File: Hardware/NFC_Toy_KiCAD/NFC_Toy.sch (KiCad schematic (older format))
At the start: 29 parts

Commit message: Ready to start layout
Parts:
- added D1, D2: LED, symbol LED
- added J10, J11, J12, J14, J3, J4, J5, J6, J7, J8, J9: TP, symbol TEST_1P
- added R1, R2: 121, symbol R
- R7: renamed from R?; value R -> 10k
- gave numbers to parts that had none: 28
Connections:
- net labels added: DotStar_Clk_3V, DotStar_Data_3V
- wire segments 132 -> 152
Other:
- note added: "Accelerometer"
- note added: "J-Link"
- note added: "Power Supply"
- note added: "uC"
- moved on the sheet: C1, C10, C11, C12, C13, C2, C3, C4, C5, C6, C7, C8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

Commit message: Layout started
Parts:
- removed J10, J11, J12, J14, J3, J4, J5, J6, J7, J8, J9: TP, symbol TEST_1P
- added TP1, TP10, TP11, TP2, TP3, TP4, TP5, TP6, TP7, TP8, TP9: TEST, NFC_Toy_Lib:Test_Point, symbol TEST
- C1, C12, C13, C2, C3, C4, C5, C6: footprint (none) -> Capacitors_SMD:C_0402
- C10, C11, C7, C8: footprint (none) -> Capacitors_SMD:C_0603_HandSoldering
- C9: footprint (none) -> Capacitors_SMD:C_1206_HandSoldering
- D1, D2: footprint (none) -> LEDs:LED_0603_HandSoldering
- J1, J2: footprint (none) -> NFC_Toy_Lib:Pad_SMD_Small
- J3: renamed from J13; footprint MODULE -> Socket_Strips:Socket_Strip_Straight_2x05_Pitch2.54mm_SMD
- L1: footprint (none) -> Inductors_SMD:L_12x12mm_h4.5mm
- R1, R10, R2, R3, R4, R5, R6, R7, R8, R9: footprint (none) -> Resistors_SMD:R_0603_HandSoldering
- U1: footprint SOP65P640X120-17N -> NFC_Toy_Lib:SOP65P640X120-17N
- U19: footprint SOT95P280X130-5N -> TO_SOT_Packages_SMD:SOT-23-5
- U2: footprint QFP50P900X900X160-48N -> NFC_Toy_Lib:QFP50P900X900X160-48N
- U3: footprint (none) -> NFC_Toy_Lib:LGA16R50P5X3_300X300X100N
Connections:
- wire segments 152 -> 151
- no-connect marks 9 -> 22
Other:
- moved on the sheet: R9

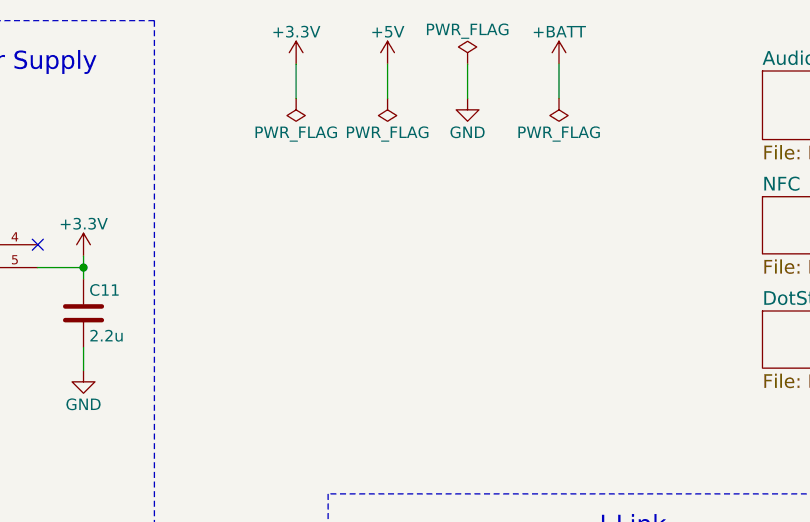
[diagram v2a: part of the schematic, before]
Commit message: Component placement complete.
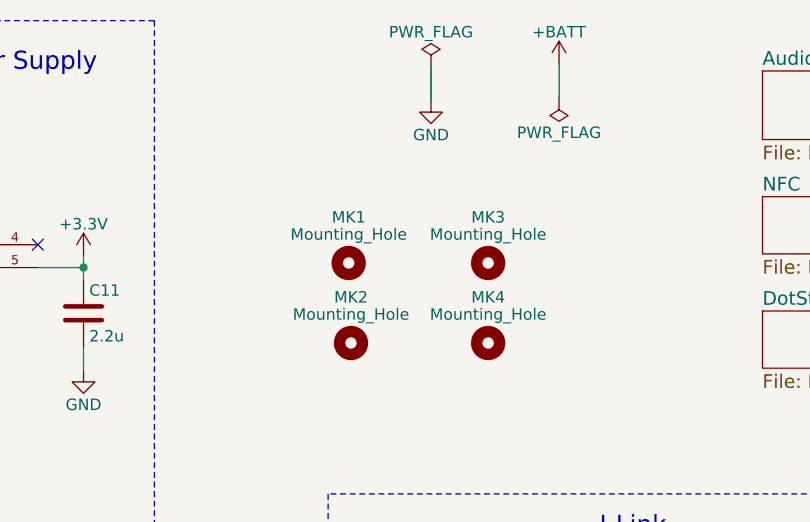
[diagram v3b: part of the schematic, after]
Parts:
- added MK1, MK2, MK3, MK4: Mounting_Hole, Mounting_Holes:MountingHole_2.5mm, symbol Mounting_Hole

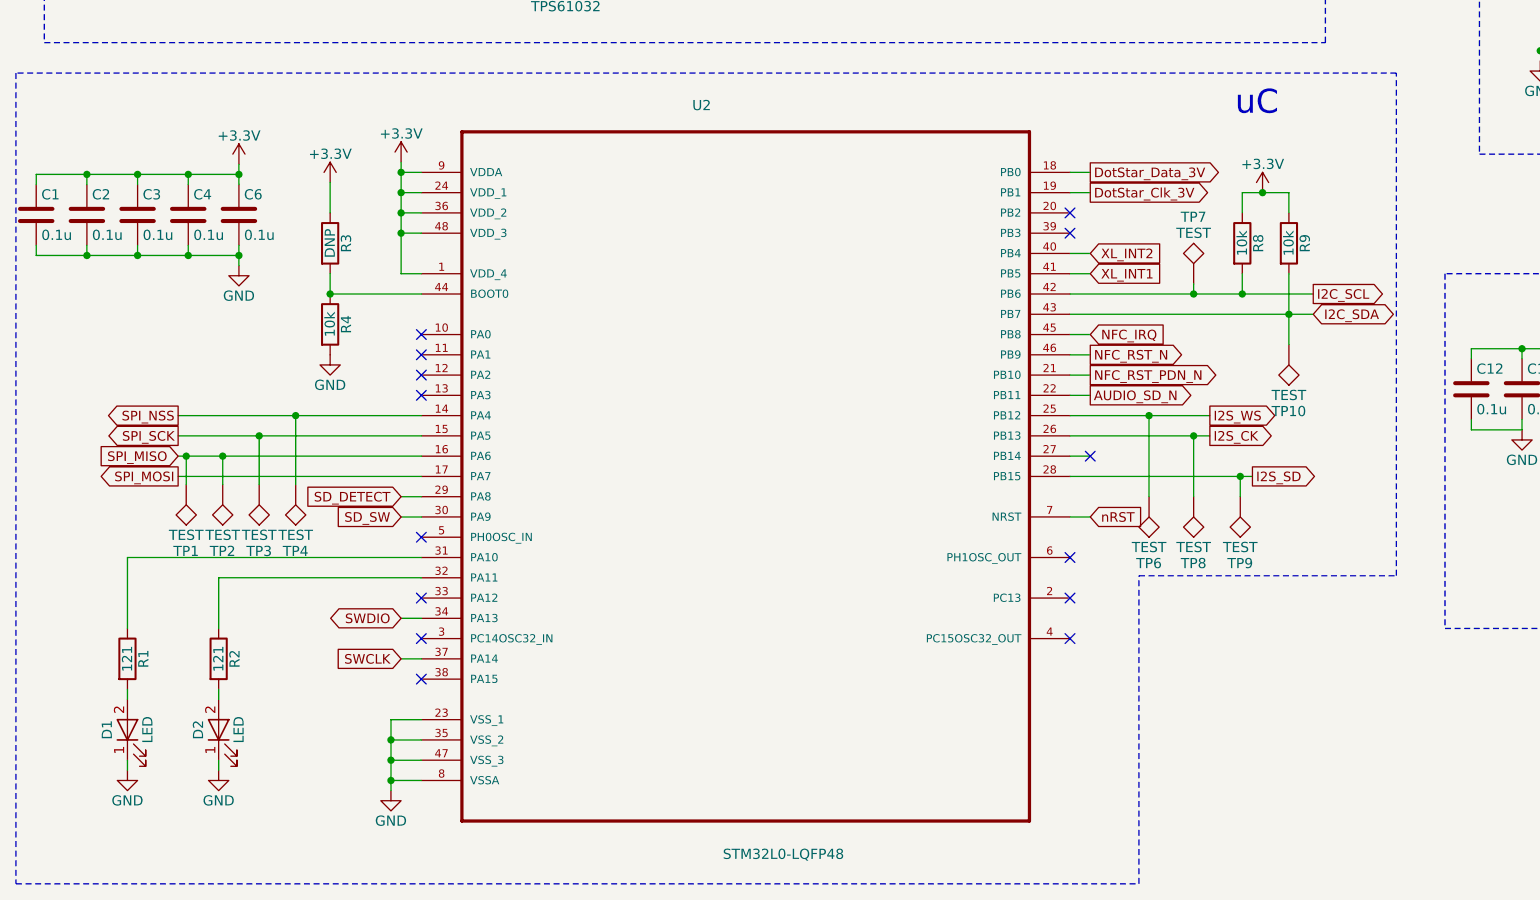
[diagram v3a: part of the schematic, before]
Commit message: Layout 75% complete
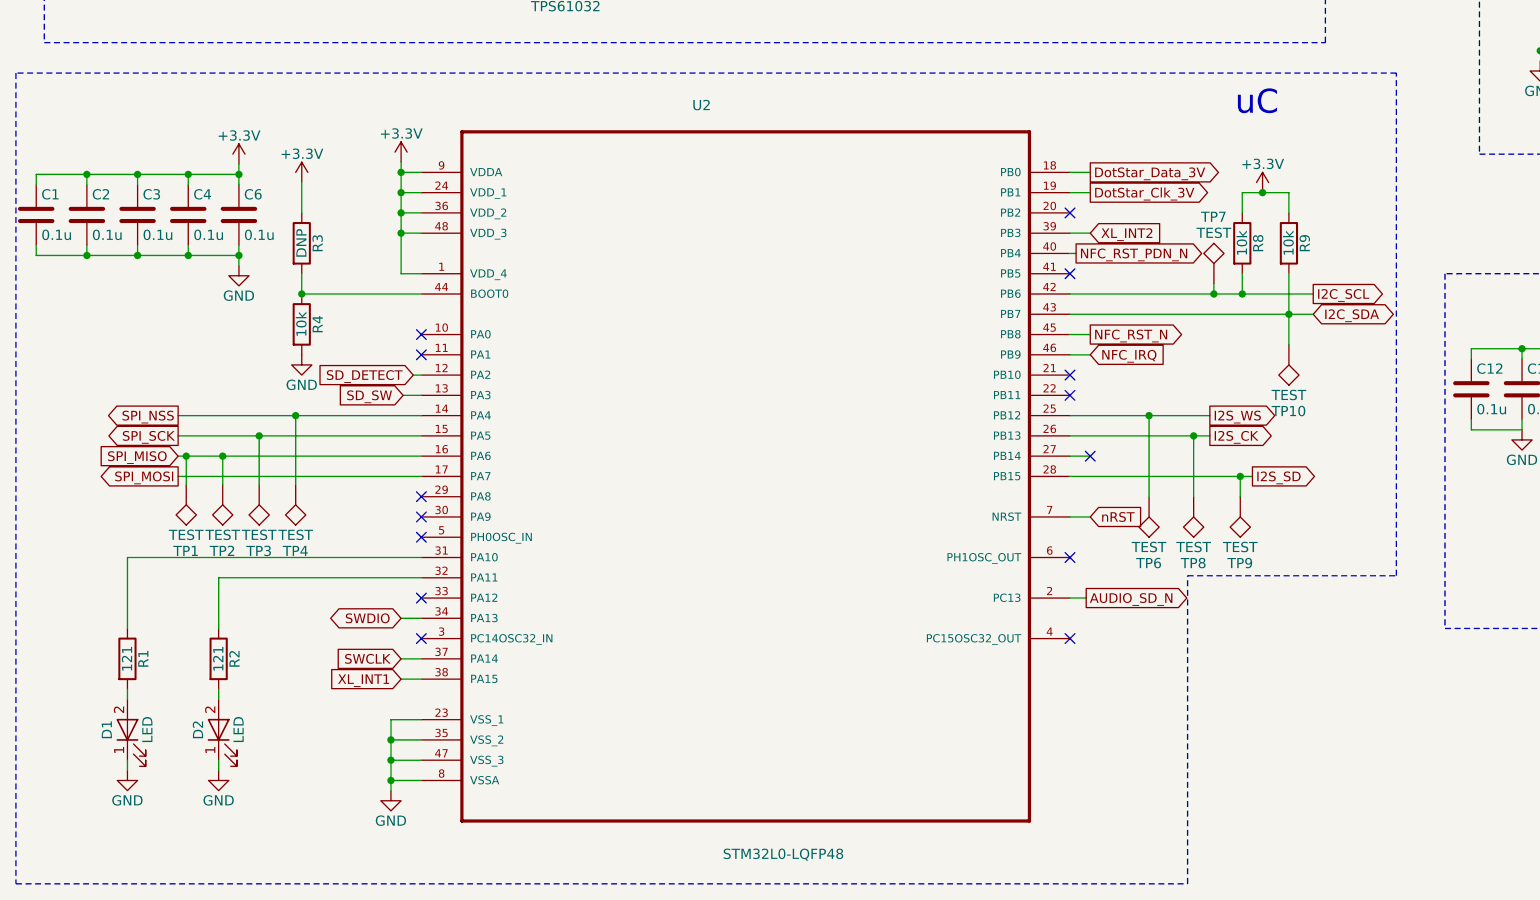
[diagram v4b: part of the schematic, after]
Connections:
- net AUDIO_SD_N: now also U2.2 (PC13); no longer U2.22 (PB11)
- net NFC_IRQ: now also U2.46 (PB9); no longer U2.45 (PB8)
- net NFC_RST_N: now also U2.45 (PB8); no longer U2.46 (PB9)
- net NFC_RST_PDN_N: now also U2.40 (PB4); no longer U2.21 (PB10)
- net SD_DETECT: now also U2.12 (PA2); no longer U2.29 (PA8)
- net SD_SW: now also U2.13 (PA3); no longer U2.30 (PA9)
- net XL_INT1: now also U2.38 (PA15); no longer U2.41 (PB5)
- net XL_INT2: now also U2.39 (PB3); no longer U2.40 (PB4)
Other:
- moved on the sheet: R3, R4, TP7
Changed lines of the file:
@@
 L R R4
 U 1 1 5AC7A59A
-P 2210 4880
-F 0 "R4" V 2290 4880 50  0000 C CNN
-F 1 "10k" V 2210 4880 50  0000 C CNN
-F 2 "Resistors_SMD:R_0603_HandSoldering" V 2140 4880 50  0001 C CNN
-F 3 "" H 2210 4880 50  0001 C CNN
-	1    2210 4880
+P 2070 4880
+F 0 "R4" V 2150 4880 50  0000 C CNN
+F 1 "10k" V 2070 4880 50  0000 C CNN
+F 2 "Resistors_SMD:R_0603_HandSoldering" V 2000 4880 50  0001 C CNN
+F 3 "" H 2070 4880 50  0001 C CNN
+	1    2070 4880
 	1    0    0    -1
 $EndComp
@@
 L R R3
 U 1 1 5ACB59B1
-P 2210 4480
-F 0 "R3" V 2290 4480 50  0000 C CNN
-F 1 "DNP" V 2210 4480 50  0000 C CNN
-F 2 "Resistors_SMD:R_0603_HandSoldering" V 2140 4480 50  0001 C CNN
-F 3 "" H 2210 4480 50  0001 C CNN
-	1    2210 4480
+P 2070 4480
+F 0 "R3" V 2150 4480 50  0000 C CNN
+F 1 "DNP" V 2070 4480 50  0000 C CNN
+F 2 "Resistors_SMD:R_0603_HandSoldering" V 2000 4480 50  0001 C CNN
+F 3 "" H 2070 4480 50  0001 C CNN
+	1    2070 4480
 	1    0    0    -1
 $EndComp
@@
 L +3.3V #PWR021
 U 1 1 5ACD275B
-P 2210 4180
-F 0 "#PWR021" H 2210 4030 50  0001 C CNN
-F 1 "+3.3V" H 2210 4320 50  0000 C CNN
-F 2 "" H 2210 4180 50  0001 C CNN
-F 3 "" H 2210 4180 50  0001 C CNN
-	1    2210 4180
+P 2070 4180
+F 0 "#PWR021" H 2070 4030 50  0001 C CNN
+F 1 "+3.3V" H 2070 4320 50  0000 C CNN
+F 2 "" H 2070 4180 50  0001 C CNN
+F 3 "" H 2070 4180 50  0001 C CNN
+	1    2070 4180
 	1    0    0    -1
 $EndComp
@@
 I2S_SD
 NoConn ~ 5960 5530
-Text GLabel 5960 5230 2    47   Output ~ 0
+Text GLabel 5940 6230 2    47   Output ~ 0
 AUDIO_SD_N
 $Sheet
@@
 L GND #PWR022
 U 1 1 5ACE0183
-P 2210 5030
-F 0 "#PWR022" H 2210 4780 50  0001 C CNN
-F 1 "GND" H 2210 4880 50  0000 C CNN
-F 2 "" H 2210 5030 50  0001 C CNN
-F 3 "" H 2210 5030 50  0001 C CNN
-	1    2210 5030
+P 2070 5030
+F 0 "#PWR022" H 2070 4780 50  0001 C CNN
+F 1 "GND" H 2070 4880 50  0000 C CNN
+F 2 "" H 2070 5030 50  0001 C CNN
+F 3 "" H 2070 5030 50  0001 C CNN
+	1    2070 5030
 	1    0    0    -1
 $EndComp
@@
 Text GLabel 1460 5630 0    47   Output ~ 0
 SPI_MOSI
-Text GLabel 2560 5730 0    47   Input ~ 0
+Text GLabel 2620 5130 0    47   Input ~ 0
 SD_DETECT
-Text GLabel 2560 5830 0    47   Input ~ 0
+Text GLabel 2570 5230 0    47   Input ~ 0
 SD_SW
 $Sheet
@@
 	1    0    0    -1
 $EndComp
-Text GLabel 5960 5030 2    47   Output ~ 0
+Text GLabel 5960 4930 2    47   Output ~ 0
 NFC_RST_N
-Text GLabel 5960 5130 2    47   Output ~ 0
+Text GLabel 5890 4530 2    47   Output ~ 0
 NFC_RST_PDN_N
-Text GLabel 5960 4930 2    47   Input ~ 0
+Text GLabel 5960 5030 2    47   Input ~ 0
 NFC_IRQ
 $Comp
@@
 NoConn ~ 10090 5300
 NoConn ~ 10090 5400
-Text GLabel 5960 4530 2    47   Input ~ 0
+Text GLabel 5960 4430 2    47   Input ~ 0
 XL_INT2
-Text GLabel 5960 4630 2    47   Input ~ 0
+Text GLabel 2560 6630 0    47   Input ~ 0
 XL_INT1
 $Comp
@@
 L TEST TP7
 U 1 1 5AD37E05
-P 6470 4680
-F 0 "TP7" H 6470 4980 50  0000 C BNN
-F 1 "TEST" H 6470 4930 50  0000 C CNN
-F 2 "NFC_Toy_Lib:Test_Point" H 6470 4680 50  0001 C CNN
-F 3 "" H 6470 4680 50  0001 C CNN
-	1    6470 4680
+P 6570 4680
+F 0 "TP7" H 6570 4980 50  0000 C BNN
+F 1 "TEST" H 6570 4930 50  0000 C CNN
+F 2 "NFC_Toy_Lib:Test_Point" H 6570 4680 50  0001 C CNN
+F 3 "" H 6570 4680 50  0001 C CNN
+	1    6570 4680
 	1    0    0    -1
 $EndComp
@@
 	9880 3730 9930 3730
 Wire Wire Line
-	2210 4630 2210 4730
+	2070 4630 2070 4730
 Wire Wire Line
 	1360 1730 2010 1730
@@
 	2010 1730 2010 1580
 Connection ~ 1660 1730
-Connection ~ 2210 4730
-Wire Wire Line
-	2210 4180 2210 4330
+Connection ~ 2070 4730
+Wire Wire Line
+	2070 4180 2070 4330
 Connection ~ 2010 1230
 Wire Wire Line
@@
 Connection ~ 6810 1730
 Wire Wire Line
-	2210 4730 2660 4730
+	2070 4730 2660 4730
 Wire Wire Line
 	2560 4430 2660 4430
@@
 	5860 5630 6760 5630
 Wire Wire Line
-	5860 5230 5960 5230
-Wire Wire Line
 	1460 5330 2660 5330
 Wire Wire Line
@@
 Wire Wire Line
 	1460 5630 2660 5630
-Wire Wire Line
-	2560 5730 2660 5730
-Wire Wire Line
-	2560 5830 2660 5830
 Wire Wire Line
 	6710 4330 6710 4230
@@
 Connection ~ 6810 4230
 Wire Wire Line
-	5960 5030 5860 5030
-Wire Wire Line
-	5860 5130 5960 5130
-Wire Wire Line
-	5960 4930 5860 4930
-Wire Wire Line
 	1760 4090 1760 4190
 Wire Wire Line
@@
 Connection ~ 8090 5000
 Wire Wire Line
-	5860 4530 5960 4530
-Wire Wire Line
-	5860 4630 5960 4630
-Wire Wire Line
 	6710 4630 6710 4730
 Connection ~ 6710 4730
@@
 Wire Notes Line
 	11110 4630 7710 4630
-Wire Wire Line
-	6470 4680 6470 4730
-Connection ~ 6470 4730
 Wire Wire Line
 	6250 5730 6250 5330
@@
 	660  3640 660  7640
 Wire Notes Line
-	660  7640 6200 7640
-Wire Notes Line
-	6200 7640 6200 6120
-Wire Notes Line
-	6200 6120 7470 6120
+	660  7640 6440 7640
+Wire Notes Line
+	6440 7640 6440 6120
+Wire Notes Line
+	6440 6120 7470 6120
 Wire Notes Line
 	7470 6120 7470 3640
@@
 	10120 5010 10120 5150
 NoConn ~ 5860 4330
-NoConn ~ 5860 4430
 NoConn ~ 5860 6030
-NoConn ~ 5860 6230
 NoConn ~ 5860 6430
-NoConn ~ 2660 6630
 NoConn ~ 2660 6430
 NoConn ~ 2660 6230
 NoConn ~ 2660 5930
-NoConn ~ 2660 5230
-NoConn ~ 2660 5130
 NoConn ~ 2660 5030
 NoConn ~ 2660 4930
@@
 Wire Wire Line
 	8330 1000 8330 850
+Wire Wire Line
+	2660 5130 2620 5130
+Wire Wire Line
+	2660 5230 2570 5230
+NoConn ~ 2660 5730
+NoConn ~ 2660 5830
+Wire Wire Line
+	5860 4430 5960 4430
+Wire Wire Line
+	2560 6630 2660 6630
+Wire Wire Line
+	6570 4680 6570 4730
+Connection ~ 6570 4730
+Wire Wire Line
+	5890 4530 5860 4530
+NoConn ~ 5860 4630
+Wire Wire Line
+	5940 6230 5860 6230
+NoConn ~ 5860 5130
+NoConn ~ 5860 5230
+Wire Wire Line
+	5960 4930 5860 4930
+Wire Wire Line
+	5960 5030 5860 5030
 $EndSCHEMATC

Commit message: First pass layout complete
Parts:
- removed TP11: TEST, NFC_Toy_Lib:Test_Point, symbol TEST
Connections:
- net SPI_MISO: no longer TP1.1
- net SPI_MOSI: now also TP1.1
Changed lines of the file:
@@
 	6700 5730 6700 5630
 Connection ~ 6700 5630
-Connection ~ 10120 5150
 Connection ~ 2560 2530
 Wire Notes Line
@@
 	1680 5670 1680 5530
 Connection ~ 1680 5530
-Wire Wire Line
-	1500 5670 1500 5530
-Connection ~ 1500 5530
 $Comp
 L TEST TP5
@@
 	1    0    0    -1
 $EndComp
-$Comp
-L TEST TP11
-U 1 1 5AD3A341
-P 10120 5010
-F 0 "TP11" H 10120 5310 50  0000 C BNN
-F 1 "TEST" H 10120 5260 50  0000 C CNN
-F 2 "NFC_Toy_Lib:Test_Point" H 10120 5010 50  0001 C CNN
-F 3 "" H 10120 5010 50  0001 C CNN
-	1    10120 5010
-	1    0    0    -1
-$EndComp
-Wire Wire Line
-	10120 5010 10120 5150
 NoConn ~ 5860 4330
 NoConn ~ 5860 6030
@@
 Wire Wire Line
 	5960 5030 5860 5030
+Wire Wire Line
+	1500 5670 1500 5630
+Connection ~ 1500 5630
 $EndSCHEMATC

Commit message: Preliminary layout complete
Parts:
- added TP11, TP16, TP17: TEST, NFC_Toy_Lib:Test_Point, symbol TEST
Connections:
- net GND: now also TP11.1, TP16.1, TP17.1
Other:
- moved on the sheet: TP5
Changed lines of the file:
@@
 	2510 1830 2710 1830
-Wire Wire Line
-	2710 2530 2560 2530
-Wire Wire Line
-	2560 2470 2560 3080
-Wire Wire Line
-	2710 2630 2560 2630
-Connection ~ 2560 2630
 Wire Wire Line
 	2710 2730 2560 2730
 Connection ~ 2560 2730
 Wire Wire Line
-	2710 2830 2560 2830
+	2560 2830 2710 2830
 Connection ~ 2560 2830
 Wire Wire Line
-	2710 3030 2560 3030
+	2560 3030 2710 3030
 Connection ~ 2560 3030
 Connection ~ 1460 1230
@@
 	6700 5730 6700 5630
 Connection ~ 6700 5630
-Connection ~ 2560 2530
 Wire Notes Line
 	660  3640 660  7640
@@
 L TEST TP5
 U 1 1 5AD39F6E
-P 2560 2470
-F 0 "TP5" H 2560 2770 50  0000 C BNN
-F 1 "TEST" H 2560 2720 50  0000 C CNN
-F 2 "NFC_Toy_Lib:Test_Point" H 2560 2470 50  0001 C CNN
-F 3 "" H 2560 2470 50  0001 C CNN
-	1    2560 2470
+P 7970 910
+F 0 "TP5" H 7970 1210 50  0000 C BNN
+F 1 "TEST" H 7970 1160 50  0000 C CNN
+F 2 "NFC_Toy_Lib:Test_Point" H 7970 910 50  0001 C CNN
+F 3 "" H 7970 910 50  0001 C CNN
+	1    7970 910
 	1    0    0    -1
 $EndComp
@@
 	1500 5670 1500 5630
 Connection ~ 1500 5630
+Wire Wire Line
+	2560 2530 2560 3080
+$Comp
+L TEST TP17
+U 1 1 5AE3537D
+P 7770 900
+F 0 "TP17" H 7770 1200 50  0000 C BNN
+F 1 "TEST" H 7770 1150 50  0000 C CNN
+F 2 "NFC_Toy_Lib:Test_Point" H 7770 900 50  0001 C CNN
+F 3 "" H 7770 900 50  0001 C CNN
+	1    7770 900
+	1    0    0    -1
+$EndComp
+$Comp
+L TEST TP16
+U 1 1 5AE3544B
+P 7570 900
+F 0 "TP16" H 7570 1200 50  0000 C BNN
+F 1 "TEST" H 7570 1150 50  0000 C CNN
+F 2 "NFC_Toy_Lib:Test_Point" H 7570 900 50  0001 C CNN
+F 3 "" H 7570 900 50  0001 C CNN
+	1    7570 900
+	1    0    0    -1
+$EndComp
+$Comp
+L TEST TP11
+U 1 1 5AE35510
+P 7380 900
+F 0 "TP11" H 7380 1200 50  0000 C BNN
+F 1 "TEST" H 7380 1150 50  0000 C CNN
+F 2 "NFC_Toy_Lib:Test_Point" H 7380 900 50  0001 C CNN
+F 3 "" H 7380 900 50  0001 C CNN
+	1    7380 900
+	1    0    0    -1
+$EndComp
+Wire Wire Line
+	7380 900  7380 970
+Wire Wire Line
+	7380 970  8330 970
+Connection ~ 8330 970
+Wire Wire Line
+	7970 910  7970 970
+Connection ~ 7970 970
+Wire Wire Line
+	7770 900  7770 970
+Connection ~ 7770 970
+Wire Wire Line
+	7570 900  7570 970
+Connection ~ 7570 970
+Wire Wire Line
+	2710 2530 2560 2530
+Wire Wire Line
+	2710 2630 2560 2630
+Connection ~ 2560 2630
 $EndSCHEMATC
